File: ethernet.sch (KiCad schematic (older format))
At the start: 32 parts, among them J3 L834-1G1T-91, U9 LAN8742A, Y3 25M

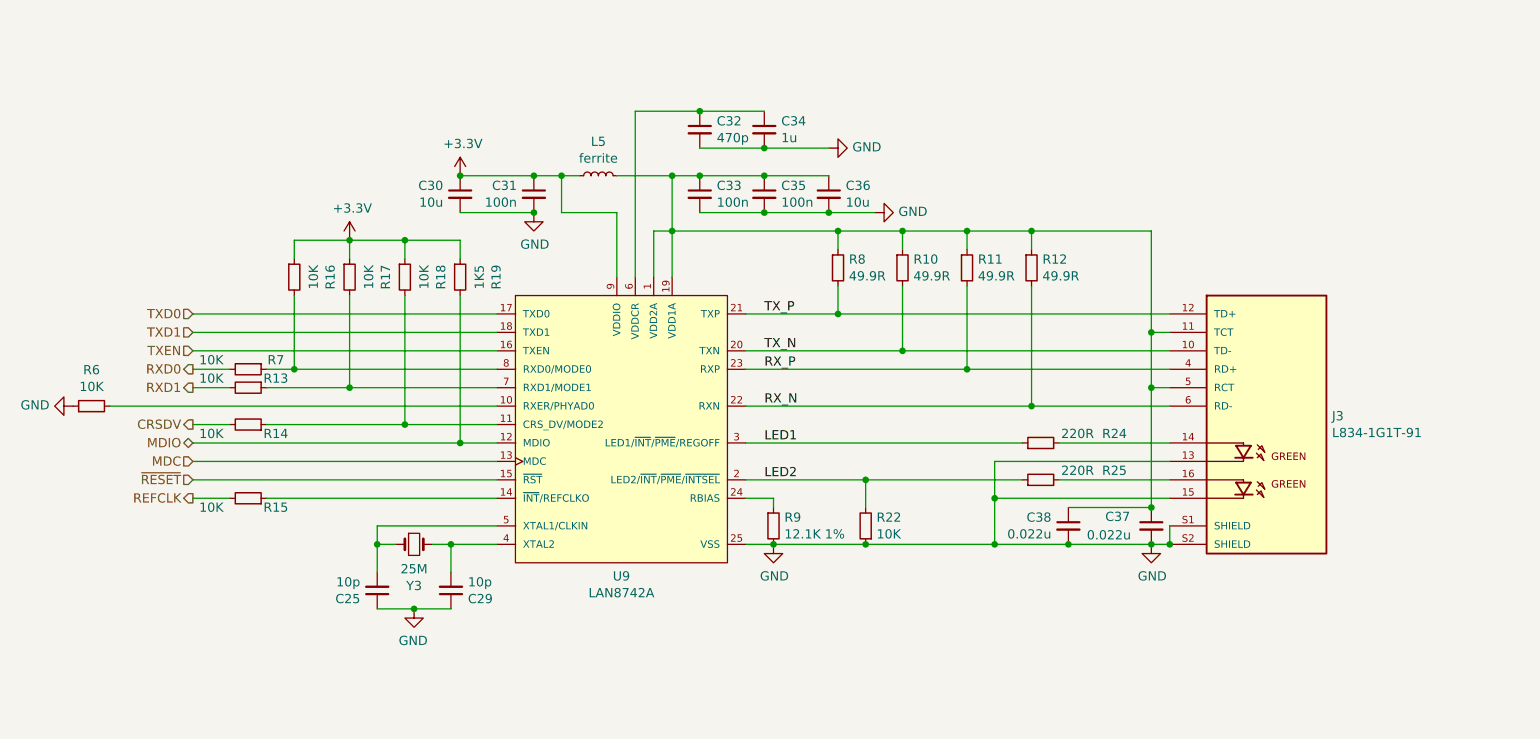
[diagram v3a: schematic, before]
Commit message: Replace LAN8742 by KSZ8081RND/RNA
Signed-off-by: Martin Ribelotta <martinribelotta@gmail.com>
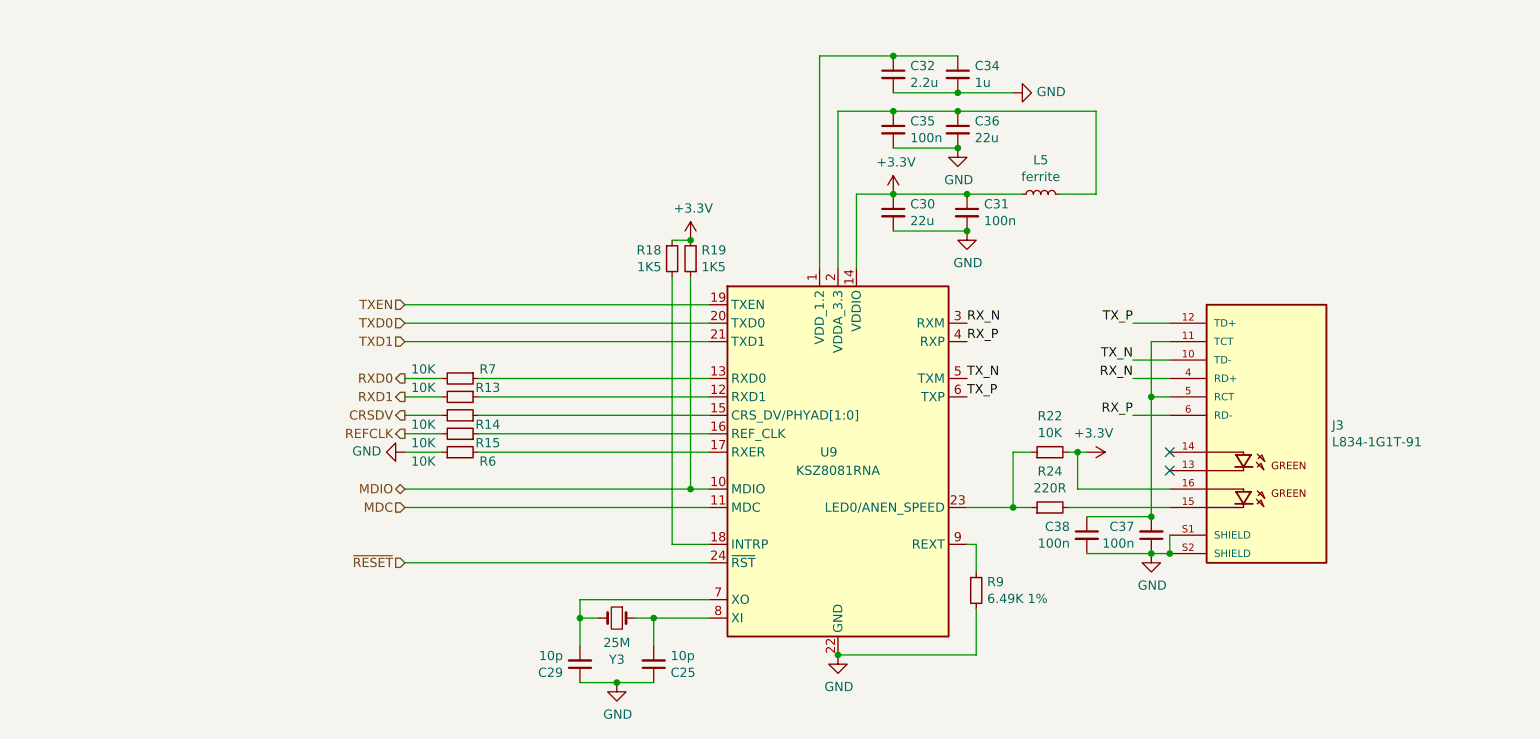
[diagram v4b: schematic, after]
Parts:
- removed C33: 100n, Capacitor_SMD:C_0603_1608Metric, symbol Device:C_Small
- removed R10, R11, R12, R8: 49.9R, Resistor_SMD:R_0603_1608Metric, symbol Device:R_Small
- removed R16, R17: 10K, Resistor_SMD:R_0603_1608Metric, symbol Device:R_Small
- removed R25: 220R, Resistor_SMD:R_0603_1608Metric, symbol Device:R_Small
- removed U9: LAN8742A, footprints:Microchip-C04-143B-S4QFN-0-0-MFG, symbol eec:LAN8742A-CZ-TR
- added U9: KSZ8081RNA, Package_DFN_QFN:QFN-24-1EP_4x4mm_P0.5mm_EP2.6x2.6mm, symbol Interface_Ethernet:KSZ8081RNA
- C30, C36: value 10u -> 22u
- C32: value 470p -> 2.2u
- C37, C38: value 0.022u -> 100n
- R18: value 10K -> 1K5
- R9: value 12.1K 1% -> 6.49K 1%
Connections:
- net LED2 is gone; now on net +3V3: R22.2
- net +3V3: now also J3.16, R19.2, U9.14 (VDDIO); no longer R19.1
- net GND: now also C37.1, U9.22 (GND), U9.25 (GND); no longer C37.2, J3.13, J3.15, R22.1
- net MDC: now also U9.11 (MDC)
- net MDIO: now also R19.1, U9.10 (MDIO); no longer R19.2
- net RX_N: now also J3.4 (RD+), U9.3 (RXM); no longer J3.6 (RD-)
- net RX_P: now also J3.6 (RD-), U9.4 (RXP); no longer J3.4 (RD+)
- net TXD0: now also U9.20 (TXD0)
- net TXD1: now also U9.21 (TXD1)
- net TXEN: now also U9.19 (TXEN)
- net TX_N: now also U9.5 (TXM)
- net TX_P: now also U9.6 (TXP)
- net ~RESET: now also U9.24 (~RST)
- net at R6.2: now also U9.17 (RXER)
- net at R14.1: now also U9.15 (CRS_DV/PHYAD[1:0]); no longer R18.2
- net at R15.1: now also U9.16 (REF_CLK)
- net at R9.1: now also U9.9 (REXT)
- net at C29.2, Y3.2: now also U9.7 (XO)
- net at C25.2, Y3.1: now also U9.8 (XI)
- net at C32.1, C34.1: now also U9.1 (VDD_1.2)
- net at R13.1: now also U9.12 (RXD1)
- net at R7.1: now also U9.13 (RXD0)
- net at R24.2: now also J3.15; no longer J3.14
- net LED1: no longer names the net of R24.1
- net LED1: now also R22.1, U9.23 (LED0/ANEN_SPEED)
- new net: C37.2, C38.1, J3.11 (TCT), J3.5 (RCT)
- new net: C35.1, C36.1, L5.2, U9.2 (VDDA_3.3)
- new net: R18.2, U9.18 (INTRP)
- no-connect marks 0 -> 2
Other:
- moved on the sheet: C25, C29, C30, C31, C32, C34, C35, C36, C37, C38, J3, L5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

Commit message: Replace STM32F042 in TSSOP by STM32F04[28] in QFN28
Others changes:

 - Export gerbers to current status
 - Update schematic export in svg and pdf
 - Update README image
 - Rename `USB OTG` sheet to `USB_OTG`

Signed-off-by: Martin Ribelotta <martinribelotta@gmail.com>
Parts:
- U9: footprint Package_DFN_QFN:QFN-24-1EP_4x4mm_P0.5mm_EP2.6x2.6mm -> Package_DFN_QFN:QFN-24-1EP_4x4mm_P0.5mm_EP2.6x2.6mm_ThermalVias
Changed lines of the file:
@@
 F 0 "U9" H 5650 4400 50  0000 C CNN
 F 1 "KSZ8081RNA" H 5700 4300 50  0000 C CNN
-F 2 "Package_DFN_QFN:QFN-24-1EP_4x4mm_P0.5mm_EP2.6x2.6mm" H 7100 3300 50  0001 C CNN
+F 2 "Package_DFN_QFN:QFN-24-1EP_4x4mm_P0.5mm_EP2.6x2.6mm_ThermalVias" H 7100 3300 50  0001 C CNN
 F 3 "http://ww1.microchip.com/downloads/en/DeviceDoc/00002199A.pdf" H 3450 4500 50  0001 C CNN
 	1    5700 4300

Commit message: Save point
Signed-off-by: Martin Ribelotta <martinribelotta@gmail.com>
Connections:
- net at C37.2, J3.5 (RCT): no longer C38.1, J3.11 (TCT)
- new net: C38.1, J3.11 (TCT)
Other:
- moved on the sheet: C37, C38, J3
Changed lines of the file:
@@
 Comment4 ""
 $EndDescr
-Wire Wire Line
-	7500 3600 7400 3600
 $Comp
 L Device:C_Small C?
 U 1 1 6019A4E1
-P 7400 4650
+P 7800 4650
 AR Path="/6019A4E1" Ref="C?"  Part="1"
 AR Path="/60185BCA/6019A4E1" Ref="C37"  Part="1"
-F 0 "C37" H 7308 4604 50  0000 R CNN
-F 1 "100n" H 7308 4695 50  0000 R CNN
-F 2 "Capacitor_SMD:C_0603_1608Metric" H 7400 4650 50  0001 C CNN
-F 3 "~" H 7400 4650 50  0001 C CNN
-F 4 "Capacitor 0.022u 0603" H 7400 4650 50  0001 C CNN "DESCRIPTION"
-F 5 "AVX" H 7400 4650 50  0001 C CNN "MANUFACTURER"
-F 6 "06035C223KAT2A" H 7400 4650 50  0001 C CNN "MANUFACTURER_PART_NUMBER"
-	1    7400 4650
+F 0 "C37" H 7708 4604 50  0000 R CNN
+F 1 "100n" H 7708 4695 50  0000 R CNN
+F 2 "Capacitor_SMD:C_0603_1608Metric" H 7800 4650 50  0001 C CNN
+F 3 "~" H 7800 4650 50  0001 C CNN
+F 4 "Capacitor 0.022u 0603" H 7800 4650 50  0001 C CNN "DESCRIPTION"
+F 5 "AVX" H 7800 4650 50  0001 C CNN "MANUFACTURER"
+F 6 "06035C223KAT2A" H 7800 4650 50  0001 C CNN "MANUFACTURER_PART_NUMBER"
+	1    7800 4650
 	1    0    0    1
 $EndComp
@@
 L power:GND #PWR050
 U 1 1 6019B07E
-P 7400 4750
-F 0 "#PWR050" H 7400 4500 50  0001 C CNN
-F 1 "GND" H 7405 4577 50  0000 C CNN
-F 2 "" H 7400 4750 50  0001 C CNN
-F 3 "" H 7400 4750 50  0001 C CNN
-	1    7400 4750
+P 7800 4750
+F 0 "#PWR050" H 7800 4500 50  0001 C CNN
+F 1 "GND" H 7805 4577 50  0000 C CNN
+F 2 "" H 7800 4750 50  0001 C CNN
+F 3 "" H 7800 4750 50  0001 C CNN
+	1    7800 4750
 	1    0    0    -1
 $EndComp
@@
 	1    0    0    -1
 $EndComp
-Connection ~ 7400 4750
+Connection ~ 7800 4750
 Wire Wire Line
 	4500 5450 4300 5450
@@
 Connection ~ 6400 3000
 Wire Wire Line
-	7050 4550 7400 4550
-Connection ~ 7400 4550
-Wire Wire Line
-	7400 4750 7050 4750
-Wire Wire Line
-	7400 3600 7400 3900
-Wire Wire Line
-	7500 3900 7400 3900
-Connection ~ 7400 3900
-Wire Wire Line
-	7400 3900 7400 4550
+	7800 4750 7450 4750
+Wire Wire Line
+	7900 3900 7800 3900
+Wire Wire Line
+	7800 3900 7800 4550
 $Comp
 L Device:C_Small C?
 U 1 1 6045B459
-P 7050 4650
+P 7450 4650
 AR Path="/6045B459" Ref="C?"  Part="1"
 AR Path="/60185BCA/6045B459" Ref="C38"  Part="1"
-F 0 "C38" H 7142 4696 50  0000 L CNN
-F 1 "100n" H 7142 4605 50  0000 L CNN
-F 2 "Capacitor_SMD:C_0603_1608Metric" H 7050 4650 50  0001 C CNN
-F 3 "~" H 7050 4650 50  0001 C CNN
-F 4 "Capacitor 0.022u 0603" H 7050 4650 50  0001 C CNN "DESCRIPTION"
-F 5 "AVX" H 7050 4650 50  0001 C CNN "MANUFACTURER"
-F 6 "06035C223KAT2A" H 7050 4650 50  0001 C CNN "MANUFACTURER_PART_NUMBER"
-	1    7050 4650
+F 0 "C38" H 7542 4696 50  0000 L CNN
+F 1 "100n" H 7542 4605 50  0000 L CNN
+F 2 "Capacitor_SMD:C_0603_1608Metric" H 7450 4650 50  0001 C CNN
+F 3 "~" H 7450 4650 50  0001 C CNN
+F 4 "Capacitor 0.022u 0603" H 7450 4650 50  0001 C CNN "DESCRIPTION"
+F 5 "AVX" H 7450 4650 50  0001 C CNN "MANUFACTURER"
+F 6 "06035C223KAT2A" H 7450 4650 50  0001 C CNN "MANUFACTURER_PART_NUMBER"
+	1    7450 4650
 	-1   0    0    -1
 $EndComp
@@
 L L834-1G1T-91:L834-1G1T-91 J3
 U 1 1 6064910E
-P 8000 4100
-F 0 "J3" H 8380 4146 50  0000 L CNN
-F 1 "L834-1G1T-91" H 8380 4055 50  0000 L CNN
-F 2 "footprints:BEL_L834-1G1T-91" H 8000 4100 50  0001 L BNN
-F 3 "" H 8000 4100 50  0001 L BNN
-F 4 "Bel Fuse" H 8000 4100 50  0001 L BNN "MANUFACTURER"
-F 5 "Manufacturer Recommendations" H 8000 4100 50  0001 L BNN "STANDARD"
-F 6 "C" H 8000 4100 50  0001 L BNN "PARTREV"
-F 7 "11.46 mm" H 8000 4100 50  0001 L BNN "MAXIMUM_PACKAGE_HEIGHT"
-F 8 "L834-1G1T-91" H 8000 4100 50  0001 C CNN "MANUFACTURER_PART_NUMBER"
-	1    8000 4100
-	1    0    0    -1
-$EndComp
-Wire Wire Line
-	7500 4750 7400 4750
-Wire Wire Line
-	7500 4650 7500 4750
-Connection ~ 7500 4750
+P 8400 4100
+F 0 "J3" H 8780 4146 50  0000 L CNN
+F 1 "L834-1G1T-91" H 8780 4055 50  0000 L CNN
+F 2 "footprints:BEL_L834-1G1T-91" H 8400 4100 50  0001 L BNN
+F 3 "" H 8400 4100 50  0001 L BNN
+F 4 "Bel Fuse" H 8400 4100 50  0001 L BNN "MANUFACTURER"
+F 5 "Manufacturer Recommendations" H 8400 4100 50  0001 L BNN "STANDARD"
+F 6 "C" H 8400 4100 50  0001 L BNN "PARTREV"
+F 7 "11.46 mm" H 8400 4100 50  0001 L BNN "MAXIMUM_PACKAGE_HEIGHT"
+F 8 "L834-1G1T-91" H 8400 4100 50  0001 C CNN "MANUFACTURER_PART_NUMBER"
+	1    8400 4100
+	1    0    0    -1
+$EndComp
+Wire Wire Line
+	7900 4750 7800 4750
+Wire Wire Line
+	7900 4650 7900 4750
+Connection ~ 7900 4750
 $Comp
 L Device:R_Small R?
@@
 Wire Wire Line
 	5600 2050 5600 3200
-Text Label 7300 3500 2    50   ~ 0
+Text Label 7700 3500 2    50   ~ 0
 TX_P
-Text Label 7300 3700 2    50   ~ 0
+Text Label 7700 3700 2    50   ~ 0
 TX_N
-Text Label 7300 4000 2    50   ~ 0
+Text Label 7700 4000 2    50   ~ 0
 RX_P
-Text Label 7300 3800 2    50   ~ 0
+Text Label 7700 3800 2    50   ~ 0
 RX_N
 Wire Wire Line
-	7300 4000 7500 4000
-Wire Wire Line
-	7500 3800 7300 3800
-Wire Wire Line
-	7300 3500 7500 3500
-Wire Wire Line
-	7500 3700 7300 3700
-NoConn ~ 7500 4300
-NoConn ~ 7500 4200
+	7700 4000 7900 4000
+Wire Wire Line
+	7900 3800 7700 3800
+Wire Wire Line
+	7700 3500 7900 3500
+Wire Wire Line
+	7900 3700 7700 3700
+NoConn ~ 7900 4300
+NoConn ~ 7900 4200
 Wire Wire Line
 	6400 4700 6450 4700
@@
 	6450 5300 6450 5050
 Connection ~ 5700 5300
-Wire Wire Line
-	6950 4500 7500 4500
 Wire Wire Line
 	6400 4500 6650 4500
@@
 Wire Wire Line
 	7000 4200 7000 4400
-Wire Wire Line
-	7000 4400 7500 4400
 Connection ~ 7000 4200
 Wire Wire Line
@@
 	4300 5000 4300 5100
 Connection ~ 4300 5100
+Wire Wire Line
+	6950 4500 7900 4500
+Wire Wire Line
+	7000 4400 7900 4400
+Wire Wire Line
+	7450 4550 7450 3600
+Wire Wire Line
+	7450 3600 7900 3600
 $EndSCHEMATC

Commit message: Change QSPI PSRAM to hyperRAM
 - Replace QSPI PSRAM to HyperBUS version due to erratasheet
   of mcu (cannot write in QSPI mode without DQS and DQS not
   work in 4bit mode)
 - Connect hyperram to QSPI interface 2
 - Move QSPI flash to interface 1
 - Rearrangue pinouts due to new functionality
 - Remove extra pinouts (now all pins are in arduino connector9
 - Improve schematic and libreries to pass ERC
 - Add pin-1 mark on all IC

Signed-off-by: Martin Ribelotta <martinribelotta@gmail.com>
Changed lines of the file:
@@
 $EndComp
 Wire Wire Line
-	5600 2050 6000 2050
+	5600 2050 5700 2050
 Connection ~ 6000 2050
 Wire Wire Line
@@
 Wire Wire Line
 	7450 3600 7900 3600
+$Comp
+L power:PWR_FLAG #FLG?
+U 1 1 607C497C
+P 5700 2050
+AR Path="/607C497C" Ref="#FLG?"  Part="1"
+AR Path="/60185BCA/607C497C" Ref="#FLG0106"  Part="1"
+F 0 "#FLG0106" H 5700 2125 50  0001 C CNN
+F 1 "PWR_FLAG" H 5700 2223 50  0000 C CNN
+F 2 "" H 5700 2050 50  0001 C CNN
+F 3 "~" H 5700 2050 50  0001 C CNN
+	1    5700 2050
+	1    0    0    -1
+$EndComp
+$Comp
+L power:PWR_FLAG #FLG?
+U 1 1 607C82CB
+P 7150 2350
+AR Path="/607C82CB" Ref="#FLG?"  Part="1"
+AR Path="/60185BCA/607C82CB" Ref="#FLG0107"  Part="1"
+F 0 "#FLG0107" H 7150 2425 50  0001 C CNN
+F 1 "PWR_FLAG" H 7150 2523 50  0000 C CNN
+F 2 "" H 7150 2350 50  0001 C CNN
+F 3 "~" H 7150 2350 50  0001 C CNN
+	1    7150 2350
+	0    1    1    0
+$EndComp
+Wire Wire Line
+	7150 2350 7100 2350
+Connection ~ 7100 2350
+Connection ~ 5700 2050
+Wire Wire Line
+	5700 2050 6000 2050
 $EndSCHEMATC

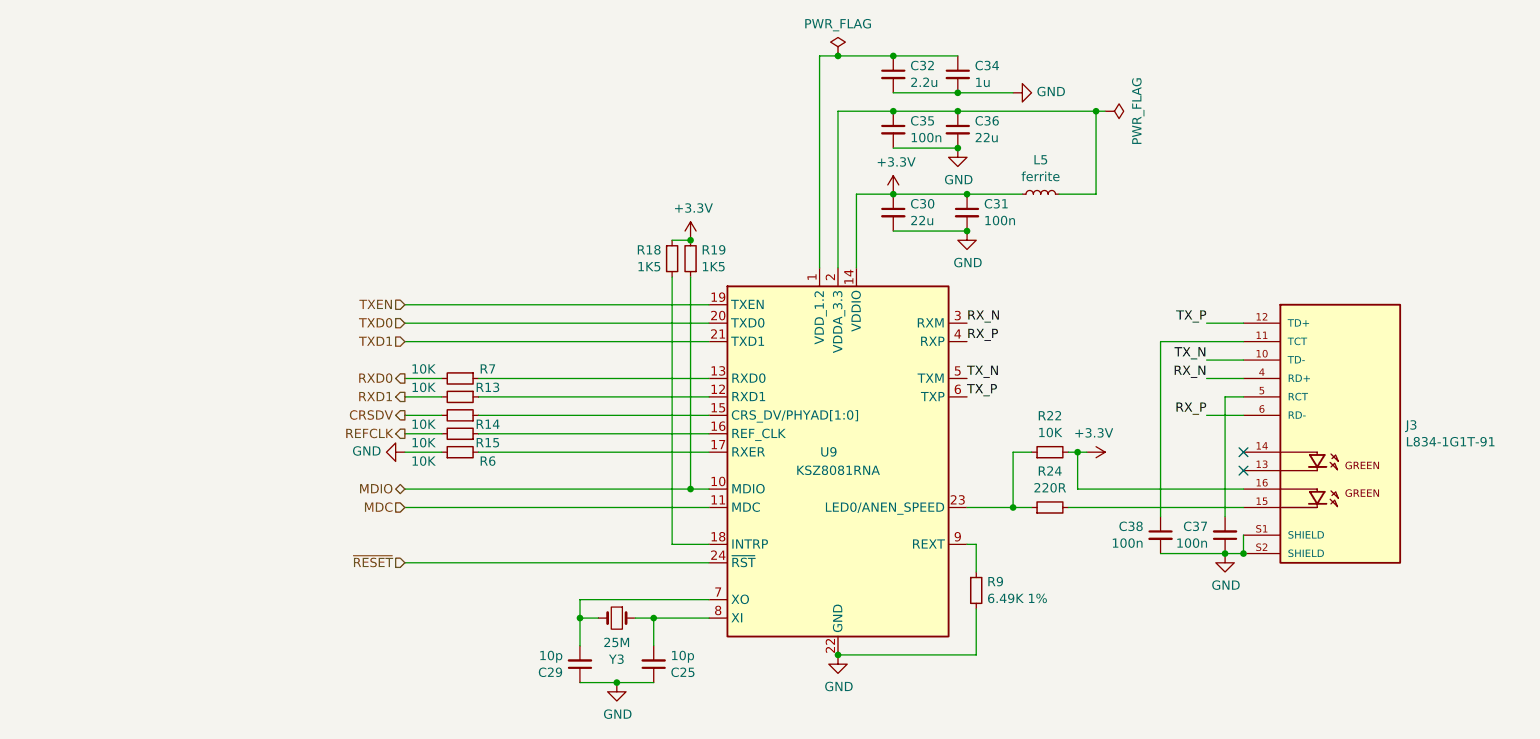
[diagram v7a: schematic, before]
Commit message: Return to lan8742A in ETH PHY
Signed-off-by: Martin Ribelotta <martinribelotta@gmail.com>
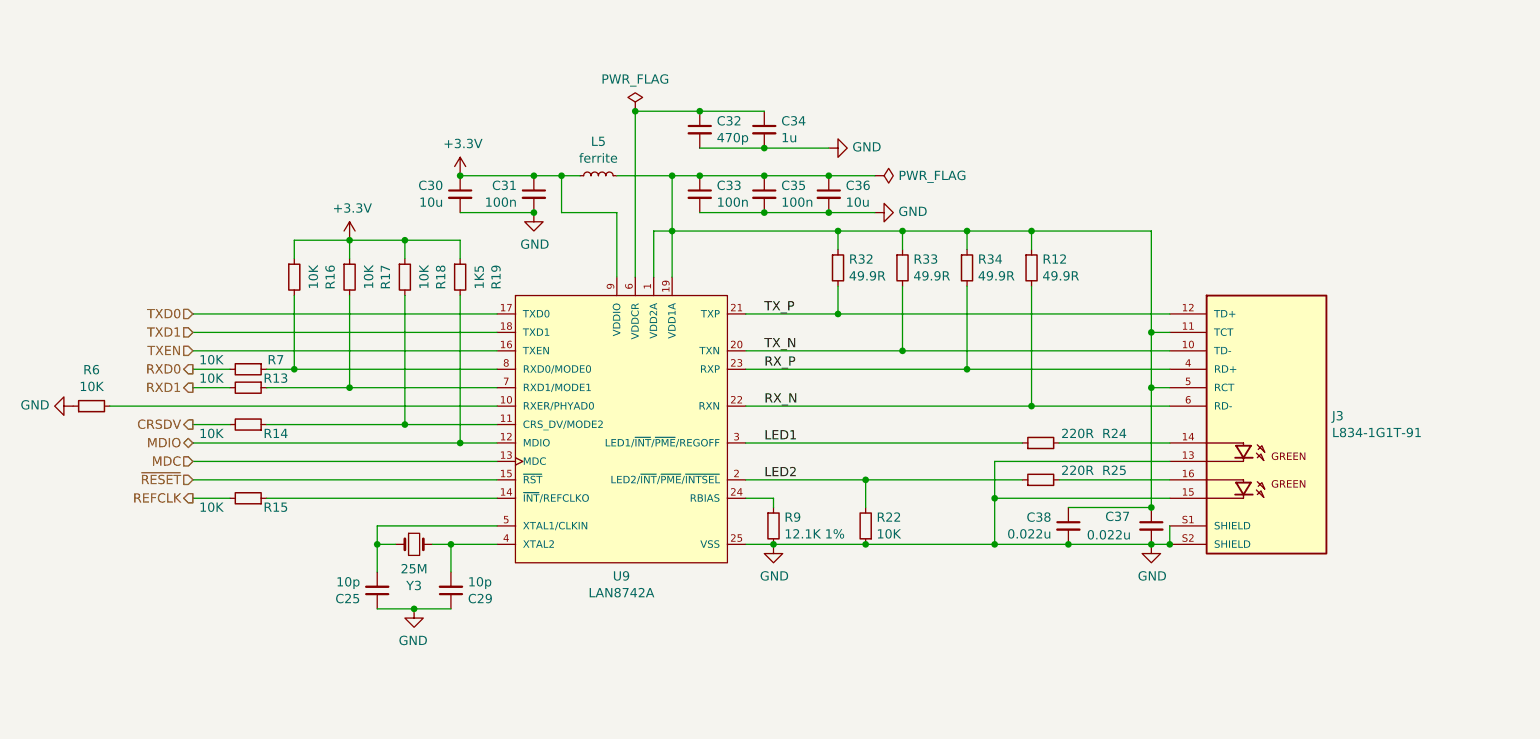
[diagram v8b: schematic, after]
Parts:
- removed U9: KSZ8081RNA, Package_DFN_QFN:QFN-24-1EP_4x4mm_P0.5mm_EP2.6x2.6mm_ThermalVias, symbol Interface_Ethernet:KSZ8081RNA
- added C33: 100n, Capacitor_SMD:C_0603_1608Metric, symbol Device:C_Small
- added R12, R32, R33, R34: 49.9R, Resistor_SMD:R_0603_1608Metric, symbol Device:R_Small
- added R16, R17: 10K, Resistor_SMD:R_0603_1608Metric, symbol Device:R_Small
- added R25: 220R, Resistor_SMD:R_0603_1608Metric, symbol Device:R_Small
- added U9: LAN8742A, footprints:Microchip-C04-143B-S4QFN-0-0-MFG, symbol eec:LAN8742A-CZ-TR
- C30, C36: value 22u -> 10u
- C32: value 2.2u -> 470p
- C37, C38: value 100n -> 0.022u
- R18: value 1K5 -> 10K
- R9: value 6.49K 1% -> 12.1K 1%
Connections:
- net +3V3: now also R19.1, R16.1, R17.1, U9.9 (VDDIO); no longer J3.16, R19.2, R22.2
- net GND: now also C37.2, J3.13, J3.15, R22.1, C33.2, U9.25 (VSS); no longer C37.1
- net MDC: now also U9.13 (MDC)
- net MDIO: now also R19.2, U9.12 (MDIO); no longer R19.1
- net RX_N: now also J3.6 (RD-), R12.2, U9.22 (RXN); no longer J3.4 (RD+)
- net RX_P: now also J3.4 (RD+), R34.2, U9.23 (RXP); no longer J3.6 (RD-)
- net TXD0: now also U9.17 (TXD0)
- net TXD1: now also U9.18 (TXD1)
- net TXEN: now also U9.16 (TXEN)
- net TX_N: now also R33.2, U9.20 (TXN)
- net TX_P: now also R32.2, U9.21 (TXP)
- net ~RESET: now also U9.15 (~RST~)
- net at J3.5 (RCT): now also C35.1, C36.1, C37.1, C38.1, J3.11 (TCT), L5.2, C33.1, R12.1, R32.1, R33.1, R34.1, U9.1 (VDD2A), U9.19 (VDD1A); no longer C37.2
- net at C32.1, C34.1: now also U9.6 (VDDCR)
- net at R9.1: now also U9.24 (RBIAS)
- net at C25.2, Y3.1: now also U9.5 (XTAL1/CLKIN)
- net at C29.2, Y3.2: now also U9.4 (XTAL2)
- net at R6.2: now also U9.10 (RXER/PHYAD0)
- net LED1: now reaches R24.1
- net LED1: now also U9.3 (LED1/~INT~/~PME~/REGOFF); no longer R22.1
- net at R24.2: now also J3.14; no longer J3.15
- net at R13.1: now also R17.2, U9.7 (RXD1/MODE1)
- net at R7.1: now also R16.2, U9.8 (RXD0/MODE0)
- net at R14.1: now also R18.2, U9.11 (CRS_DV/MODE2)
- net at R15.1: now also U9.14 (~INT~/REFCLKO)
- new net: J3.16, R25.2
- new net LED2: R22.2, R25.1, U9.2 (LED2/~INT~/~PME~/~INTSEL~)
- no-connect marks 2 -> 0
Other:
- moved on the sheet: C25, C29, C30, C31, C32, C34, C35, C36, C37, C38, J3, L5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
